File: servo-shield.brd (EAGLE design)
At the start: 65 x 56 mm, 23 parts, among them IC1 24AA01P, K1 PIN20X2

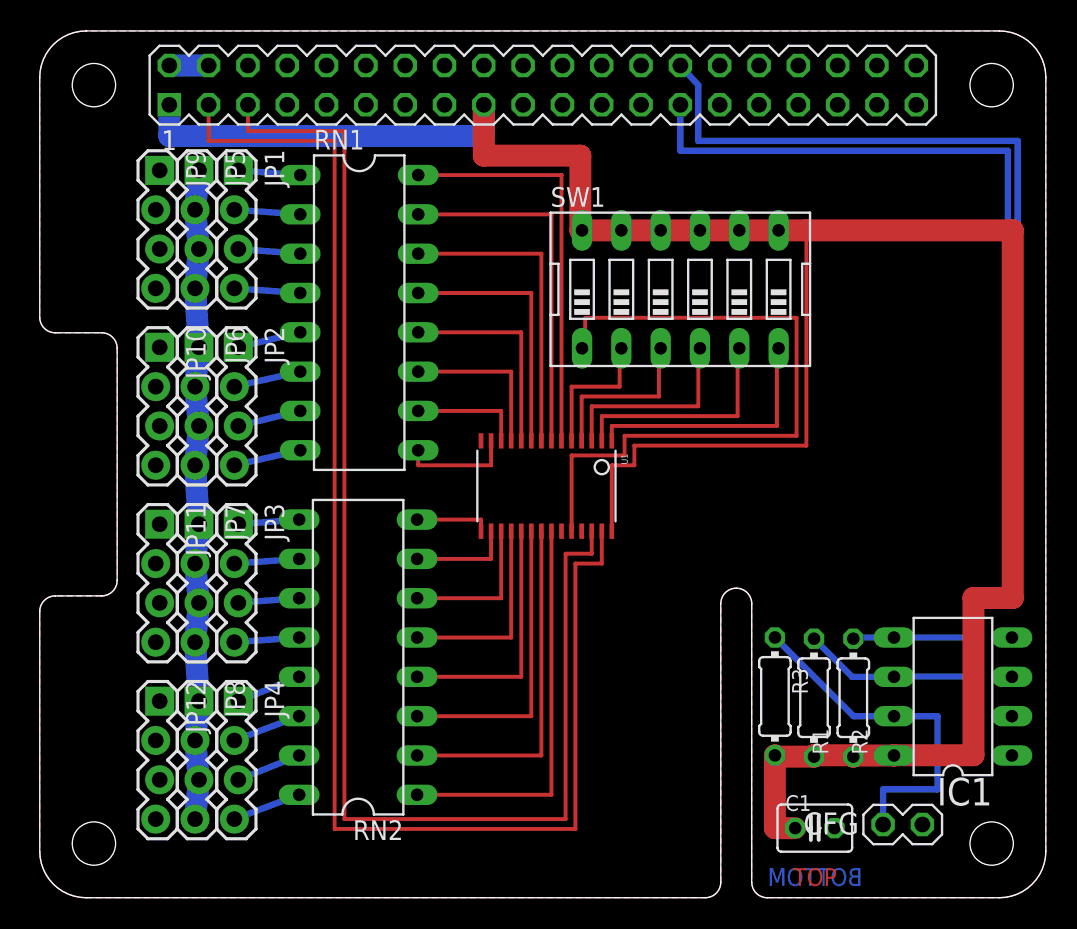
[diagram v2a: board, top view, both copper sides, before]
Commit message: Added power connector + regulator
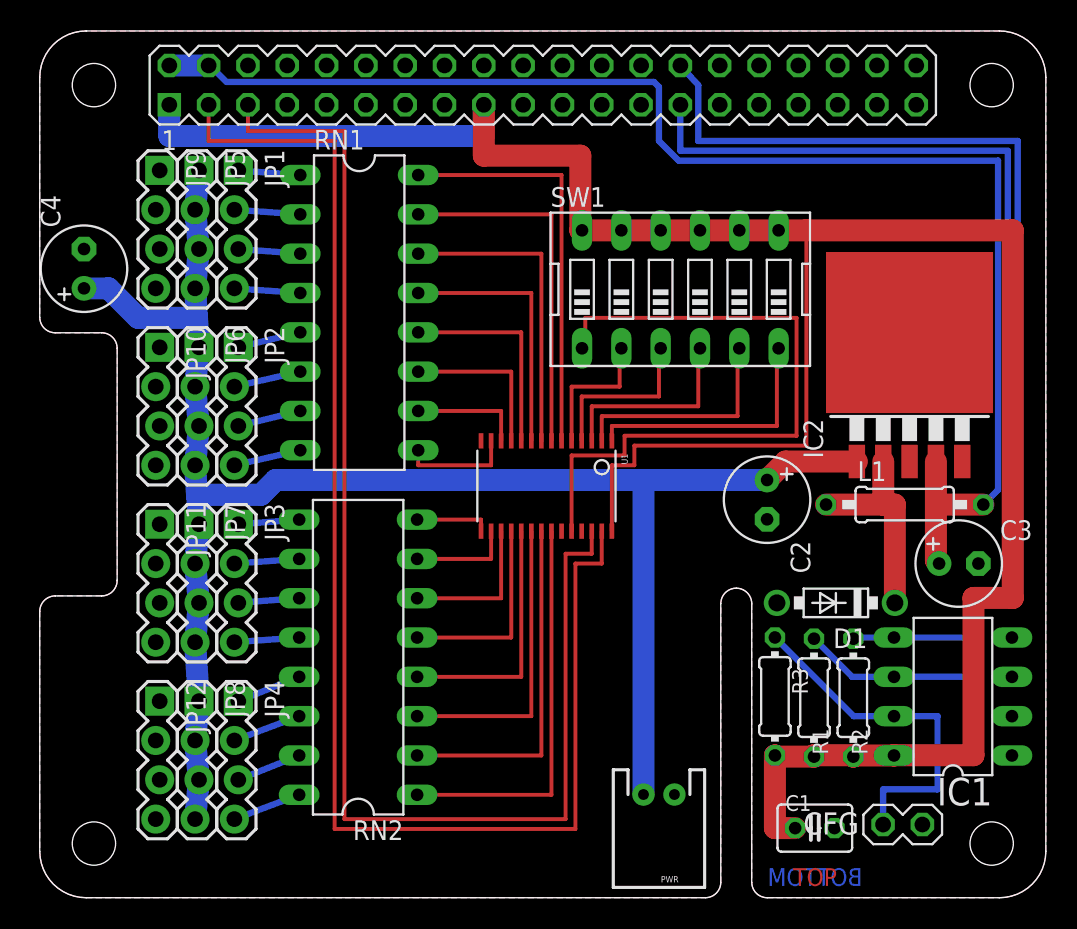
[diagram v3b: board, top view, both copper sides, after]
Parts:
- added C2: 680uf, rcl:E2,5-6
- added C3: 220uf, rcl:E2,5-6
- added C4: 640uf, rcl:E2,5-6
- added D1: 1N5824, diode:DO41-7.6
- added IC2: (no value), linear:TO263-5
- added L1: 33uh, rcl:0207/10
- added PWR: (no value), SparkFun-Connectors:JST-2-PTH
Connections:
- new net N$40: D1.C, IC2.2, L1.1
- net +5V: now also C3.+, IC2.4, L1.2
- net GND: now also C2.-, C3.-, C4.-, D1.A, IC2.3, IC2.5, IC2.6, PWR.1
- net V+: now also C2.+, C4.+, IC2.1, PWR.2
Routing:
- net +5V: track 2.54 -> 90.5 mm
- net V+: track 42.1 -> 114.2 mm
- net N$40: track 0.00 -> 13.6 mm
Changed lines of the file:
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@@
 <element name="JP11" library="SparkFun-Connectors" package="1X04_LOCK" value="" x="7.62" y="24.13" rot="R270"/>
 <element name="JP12" library="SparkFun-Connectors" package="1X04_LOCK" value="" x="7.62" y="12.7" rot="R270"/>
+<element name="IC2" library="linear" package="TO263-5" value="" x="56.1975" y="33.9725"/>
+<element name="C2" library="rcl" package="E2,5-6" value="680uf" x="46.99" y="25.7175" rot="R270"/>
+<element name="L1" library="rcl" package="0207/10" value="33uh" x="55.88" y="25.4"/>
+<element name="D1" library="diode" package="DO41-7.6" value="1N5824" x="51.435" y="19.05" rot="R180"/>
+<element name="C3" library="rcl" package="E2,5-6" value="220uf" x="59.3725" y="21.59"/>
+<element name="C4" library="rcl" package="E2,5-6" value="640uf" x="2.8575" y="40.64" rot="R90"/>
+<element name="PWR" library="SparkFun-Connectors" package="JST-2-PTH" value="" x="40.005" y="6.6675" rot="R180">
+<attribute name="SKU" value="PRT-09914" x="40.005" y="6.6675" size="1.778" layer="27" rot="R180" display="off"/>
+</element>
 </elements>
 <signals>
@@
 <contactref element="JP12" pad="3"/>
 <contactref element="JP12" pad="4"/>
+<contactref element="IC2" pad="6"/>
+<contactref element="IC2" pad="5"/>
+<contactref element="IC2" pad="3"/>
+<contactref element="IC2" pad="6"/>
+<contactref element="C2" pad="-"/>
+<contactref element="D1" pad="A"/>
+<contactref element="C3" pad="-"/>
+<contactref element="C4" pad="-"/>
+<contactref element="PWR" pad="1"/>
 </signal>
 <signal name="+3V3">
@@
 <contactref element="K1" pad="4"/>
 <wire x1="8.37" y1="53.77" x2="10.91" y2="53.77" width="1.4224" layer="16"/>
+<contactref element="L1" pad="2"/>
+<contactref element="IC2" pad="4"/>
+<contactref element="C3" pad="+"/>
+<wire x1="57.8993" y1="28.1813" x2="57.8993" y2="25.4" width="1.4224" layer="1"/>
+<wire x1="57.8993" y1="25.4" x2="60.96" y2="25.4" width="1.4224" layer="1"/>
+<wire x1="57.8993" y1="25.4" x2="57.8993" y2="21.7932" width="1.4224" layer="1"/>
+<wire x1="57.8993" y1="21.7932" x2="58.1025" y2="21.59" width="1.4224" layer="1"/>
+<wire x1="10.91" y1="53.77" x2="11" y2="53.77" width="0.4064" layer="16"/>
+<wire x1="11" y1="53.77" x2="12.065" y2="52.705" width="0.4064" layer="16"/>
+<wire x1="12.065" y1="52.705" x2="39.6875" y2="52.705" width="0.4064" layer="16"/>
+<wire x1="39.6875" y1="52.705" x2="40.005" y2="52.3875" width="0.4064" layer="16"/>
+<wire x1="40.005" y1="52.3875" x2="40.005" y2="48.895" width="0.4064" layer="16"/>
+<wire x1="40.005" y1="48.895" x2="41.275" y2="47.625" width="0.4064" layer="16"/>
+<wire x1="41.275" y1="47.625" x2="61.9125" y2="47.625" width="0.4064" layer="16"/>
+<wire x1="61.9125" y1="47.625" x2="61.9125" y2="26.3525" width="0.4064" layer="16"/>
+<wire x1="61.9125" y1="26.3525" x2="60.96" y2="25.4" width="0.4064" layer="16"/>
 </signal>
 <signal name="N$4">
@@
 <wire x1="10.287" y1="30.48" x2="10.033" y2="33.02" width="1.4224" layer="16"/>
 <wire x1="10.033" y1="33.02" x2="10.287" y2="35.56" width="1.4224" layer="16"/>
-<wire x1="10.033" y1="27.94" x2="10.287" y2="24.13" width="1.4224" layer="16"/>
+<wire x1="10.033" y1="27.94" x2="10.162809375" y2="25.992853125" width="1.4224" layer="16"/>
+<wire x1="10.162809375" y1="25.992853125" x2="10.287" y2="24.13" width="1.4224" layer="16"/>
 <wire x1="10.287" y1="24.13" x2="10.033" y2="21.59" width="1.4224" layer="16"/>
 <wire x1="10.033" y1="21.59" x2="10.287" y2="19.05" width="1.4224" layer="16"/>
@@
 <wire x1="10.033" y1="10.16" x2="10.287" y2="12.7" width="1.4224" layer="16"/>
 <wire x1="10.287" y1="12.7" x2="10.033" y2="16.51" width="1.4224" layer="16"/>
-<wire x1="10.287" y1="35.56" x2="10.033" y2="39.37" width="1.4224" layer="16"/>
+<wire x1="10.287" y1="35.56" x2="10.157190625" y2="37.507146875" width="1.4224" layer="16"/>
+<wire x1="10.157190625" y1="37.507146875" x2="10.033" y2="39.37" width="1.4224" layer="16"/>
 <wire x1="10.033" y1="39.37" x2="10.287" y2="41.91" width="1.4224" layer="16"/>
 <wire x1="10.287" y1="41.91" x2="10.033" y2="44.45" width="1.4224" layer="16"/>
 <wire x1="10.033" y1="44.45" x2="10.287" y2="46.99" width="1.4224" layer="16"/>
+<contactref element="IC2" pad="1"/>
+<contactref element="C2" pad="+"/>
+<contactref element="C4" pad="+"/>
+<wire x1="2.8575" y1="39.37" x2="4.445" y2="39.37" width="1.4224" layer="16"/>
+<wire x1="4.445" y1="39.37" x2="6.35" y2="37.465" width="1.4224" layer="16"/>
+<wire x1="6.35" y1="37.465" x2="10.11504375" y2="37.465" width="1.4224" layer="16"/>
+<wire x1="10.11504375" y1="37.465" x2="10.157190625" y2="37.507146875" width="1.4224" layer="16"/>
+<wire x1="52.7939" y1="28.1813" x2="48.1838" y2="28.1813" width="1.4224" layer="1"/>
+<wire x1="48.1838" y1="28.1813" x2="46.99" y2="26.9875" width="1.4224" layer="1"/>
+<wire x1="46.99" y1="26.9875" x2="38.735" y2="26.9875" width="1.4224" layer="16"/>
+<wire x1="38.735" y1="26.9875" x2="15.24" y2="26.9875" width="1.4224" layer="16"/>
+<wire x1="15.24" y1="26.9875" x2="14.2875" y2="26.035" width="1.4224" layer="16"/>
+<wire x1="14.2875" y1="26.035" x2="10.20495625" y2="26.035" width="1.4224" layer="16"/>
+<wire x1="10.20495625" y1="26.035" x2="10.162809375" y2="25.992853125" width="1.4224" layer="16"/>
+<contactref element="PWR" pad="2"/>
+<wire x1="39.005" y1="6.6675" x2="39.005" y2="26.7175" width="1.4224" layer="16"/>
+<wire x1="39.005" y1="26.7175" x2="38.735" y2="26.9875" width="1.4224" layer="16"/>
+</signal>
+<signal name="N$40">
+<contactref element="IC2" pad="2"/>
+<contactref element="L1" pad="1"/>
+<contactref element="D1" pad="C"/>
+<wire x1="54.4957" y1="28.1813" x2="54.4957" y2="25.4" width="1.4224" layer="1"/>
+<wire x1="50.8" y1="25.4" x2="54.4957" y2="25.4" width="1.4224" layer="1"/>
+<wire x1="54.4957" y1="25.4" x2="55.245" y2="25.4" width="1.4224" layer="1"/>
+<wire x1="55.245" y1="25.4" x2="55.245" y2="19.05" width="1.4224" layer="1"/>
 </signal>
 </signals>

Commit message: Moved some parts and labels around
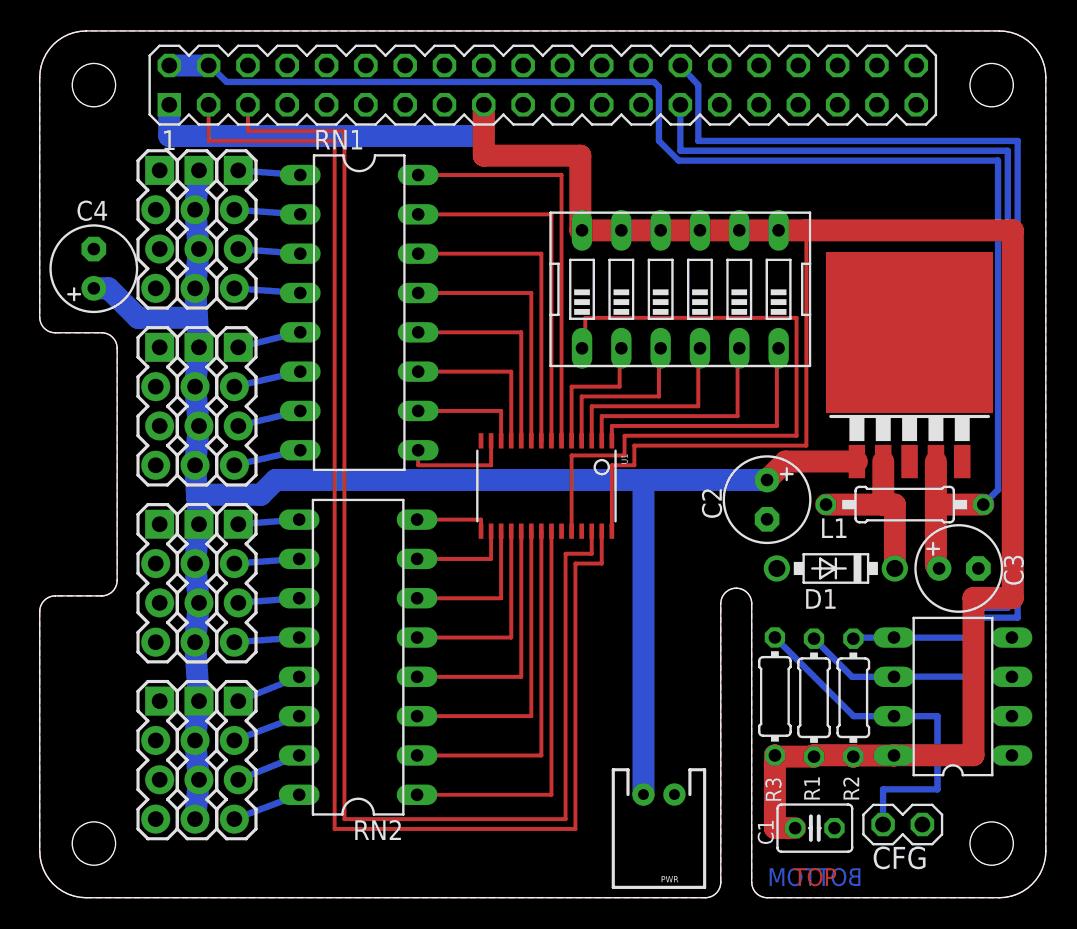
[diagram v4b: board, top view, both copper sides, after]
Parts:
- moved D1 2.22 mm to (51.4, 21.3)
- moved C4 0.64 mm to (3.49, 40.6)
- moved C3 0.32 mm to (59.4, 21.3)
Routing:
- net N$40: track 13.6 -> 11.4 mm
- net V+: track 114.2 -> 113.5 mm
